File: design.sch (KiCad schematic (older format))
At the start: 5 parts, among them J1 USB_C_Receptacle, J2 Conn_01x05, U1 ATtiny1616-M

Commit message: Update design.sch
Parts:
- added U?: ATtiny1616-M, Package_DFN_QFN:VQFN-20-1EP_3x3mm_P0.4mm_EP1.7x1.7mm, symbol MCU_Microchip_ATtiny:ATtiny1616-M
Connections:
- new net: U?.21 (GND), U?.3 (GND)
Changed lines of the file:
@@
+	1    0    0    -1
+$EndComp
+$Comp
+L MCU_Microchip_ATtiny:ATtiny1616-M U?
+U 1 1 617108F0
+P 5000 5750
+F 0 "U?" H 5000 6831 50  0000 C CNN
+F 1 "ATtiny1616-M" H 5000 6740 50  0000 C CNN
+F 2 "Package_DFN_QFN:VQFN-20-1EP_3x3mm_P0.4mm_EP1.7x1.7mm" H 5000 5750 50  0001 C CIN
+F 3 "http://ww1.microchip.com/downloads/en/DeviceDoc/ATtiny3216_ATtiny1616-data-sheet-40001997B.pdf" H 5000 5750 50  0001 C CNN
+	1    5000 5750
 	1    0    0    -1
 $EndComp

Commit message: Update design.sch
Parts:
- added U?: ATtiny1616-M, Package_DFN_QFN:VQFN-20-1EP_3x3mm_P0.4mm_EP1.7x1.7mm, symbol MCU_Microchip_ATtiny:ATtiny1616-M
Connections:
- new net: U?.21 (GND), U?.3 (GND)
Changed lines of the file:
@@
+	1    0    0    -1
+$EndComp
+$Comp
+L MCU_Microchip_ATtiny:ATtiny1616-M U?
+U 1 1 61711161
+P 6750 5375
+F 0 "U?" H 6750 6456 50  0000 C CNN
+F 1 "ATtiny1616-M" H 6750 6365 50  0000 C CNN
+F 2 "Package_DFN_QFN:VQFN-20-1EP_3x3mm_P0.4mm_EP1.7x1.7mm" H 6750 5375 50  0001 C CIN
+F 3 "http://ww1.microchip.com/downloads/en/DeviceDoc/ATtiny3216_ATtiny1616-data-sheet-40001997B.pdf" H 6750 5375 50  0001 C CNN
+	1    6750 5375
 	1    0    0    -1
 $EndComp

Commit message: Update design.sch
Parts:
- removed U? (x2): ATtiny1616-M, Package_DFN_QFN:VQFN-20-1EP_3x3mm_P0.4mm_EP1.7x1.7mm, symbol MCU_Microchip_ATtiny:ATtiny1616-M
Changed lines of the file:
@@
-	1    0    0    -1
-$EndComp
-$Comp
-L MCU_Microchip_ATtiny:ATtiny1616-M U?
-U 1 1 617108F0
-P 5000 5750
-F 0 "U?" H 5000 6831 50  0000 C CNN
-F 1 "ATtiny1616-M" H 5000 6740 50  0000 C CNN
-F 2 "Package_DFN_QFN:VQFN-20-1EP_3x3mm_P0.4mm_EP1.7x1.7mm" H 5000 5750 50  0001 C CIN
-F 3 "http://ww1.microchip.com/downloads/en/DeviceDoc/ATtiny3216_ATtiny1616-data-sheet-40001997B.pdf" H 5000 5750 50  0001 C CNN
-	1    5000 5750
-	1    0    0    -1
-$EndComp
-$Comp
-L MCU_Microchip_ATtiny:ATtiny1616-M U?
-U 1 1 61711161
-P 6750 5375
-F 0 "U?" H 6750 6456 50  0000 C CNN
-F 1 "ATtiny1616-M" H 6750 6365 50  0000 C CNN
-F 2 "Package_DFN_QFN:VQFN-20-1EP_3x3mm_P0.4mm_EP1.7x1.7mm" H 6750 5375 50  0001 C CIN
-F 3 "http://ww1.microchip.com/downloads/en/DeviceDoc/ATtiny3216_ATtiny1616-data-sheet-40001997B.pdf" H 6750 5375 50  0001 C CNN
-	1    6750 5375
 	1    0    0    -1
 $EndComp

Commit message: k
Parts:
- added U?: AD1853, Package_SO:SSOP-28_5.3x10.2mm_P0.65mm, symbol Audio:AD1853
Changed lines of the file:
@@
+	1    0    0    -1
+$EndComp
+$Comp
+L Audio:AD1853 U?
+U 1 1 6174A6D7
+P 9400 2700
+F 0 "U?" H 9400 3781 50  0000 C CNN
+F 1 "AD1853" H 9400 3690 50  0000 C CNN
+F 2 "Package_SO:SSOP-28_5.3x10.2mm_P0.65mm" H 9850 1700 50  0001 C CNN
+F 3 "https://www.analog.com/media/en/technical-documentation/data-sheets/AD1853.pdf" H 9400 2700 50  0001 C CNN
+	1    9400 2700
 	1    0    0    -1
 $EndComp

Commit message: Update design.sch
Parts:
- added U2: ADP5063, Package_DFN_QFN:QFN-20-1EP_4x4mm_P0.5mm_EP2.5x2.5mm, symbol Battery_Management:ADP5063
- gave numbers to parts that had none: 1
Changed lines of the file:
@@
 $EndComp
 $Comp
-L Audio:AD1853 U?
+L Audio:AD1853 U3
 U 1 1 6174A6D7
 P 9400 2700
-F 0 "U?" H 9400 3781 50  0000 C CNN
+F 0 "U3" H 9400 3781 50  0000 C CNN
 F 1 "AD1853" H 9400 3690 50  0000 C CNN
 F 2 "Package_SO:SSOP-28_5.3x10.2mm_P0.65mm" H 9850 1700 50  0001 C CNN
@@
 	1    0    0    -1
 $EndComp
+$Comp
+L Battery_Management:ADP5063 U2
+U 1 1 6174B0B1
+P 1300 1675
+F 0 "U2" H 1300 2442 50  0000 C CNN
+F 1 "ADP5063" H 1300 2351 50  0000 C CNN
+F 2 "Package_DFN_QFN:QFN-20-1EP_4x4mm_P0.5mm_EP2.5x2.5mm" H 1550 775 50  0001 C CNN
+F 3 "https://www.analog.com/media/en/technical-documentation/data-sheets/ADP5063.pdf" H -900 3125 50  0001 C CNN
+	1    1300 1675
+	1    0    0    -1
+$EndComp

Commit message: test
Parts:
- removed U2: ADP5063, Package_DFN_QFN:QFN-20-1EP_4x4mm_P0.5mm_EP2.5x2.5mm, symbol Battery_Management:ADP5063
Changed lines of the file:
@@
-	1    0    0    -1
-$EndComp
-$Comp
-L Battery_Management:ADP5063 U2
-U 1 1 6174B0B1
-P 1300 1675
-F 0 "U2" H 1300 2442 50  0000 C CNN
-F 1 "ADP5063" H 1300 2351 50  0000 C CNN
-F 2 "Package_DFN_QFN:QFN-20-1EP_4x4mm_P0.5mm_EP2.5x2.5mm" H 1550 775 50  0001 C CNN
-F 3 "https://www.analog.com/media/en/technical-documentation/data-sheets/ADP5063.pdf" H -900 3125 50  0001 C CNN
-	1    1300 1675
 	1    0    0    -1
 $EndComp

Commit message: update sch
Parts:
- removed U3: AD1853, Package_SO:SSOP-28_5.3x10.2mm_P0.65mm, symbol Audio:AD1853
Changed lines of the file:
@@
-	1    0    0    -1
-$EndComp
-$Comp
-L Audio:AD1853 U3
-U 1 1 6174A6D7
-P 9400 2700
-F 0 "U3" H 9400 3781 50  0000 C CNN
-F 1 "AD1853" H 9400 3690 50  0000 C CNN
-F 2 "Package_SO:SSOP-28_5.3x10.2mm_P0.65mm" H 9850 1700 50  0001 C CNN
-F 3 "https://www.analog.com/media/en/technical-documentation/data-sheets/AD1853.pdf" H 9400 2700 50  0001 C CNN
-	1    9400 2700
 	1    0    0    -1
 $EndComp

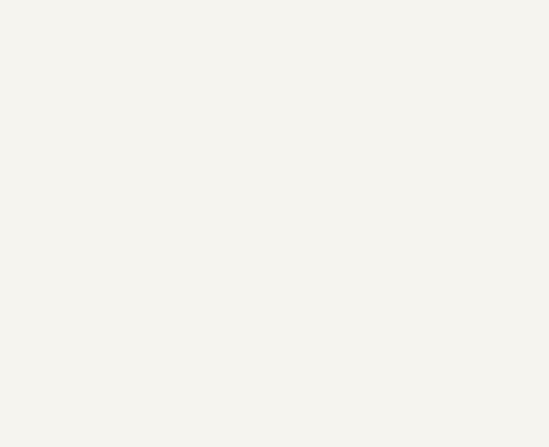
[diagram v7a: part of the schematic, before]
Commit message: add test component
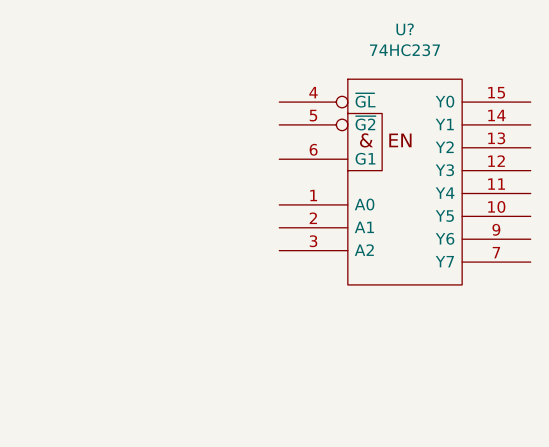
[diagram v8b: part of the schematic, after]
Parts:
- added U?: 74HC237, symbol 74xx_IEEE:74HC237
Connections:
- new net GND: U?.8 (GND)
- new net VCC: U?.16 (VCC)
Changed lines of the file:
@@
+	1    0    0    -1
+$EndComp
+$Comp
+L 74xx_IEEE:74HC237 U?
+U 1 1 61745050
+P 9025 2075
+F 0 "U?" H 9025 2591 50  0000 C CNN
+F 1 "74HC237" H 9025 2500 50  0000 C CNN
+F 2 "" H 9025 2075 50  0001 C CNN
+F 3 "" H 9025 2075 50  0001 C CNN
+	1    9025 2075
 	1    0    0    -1
 $EndComp
